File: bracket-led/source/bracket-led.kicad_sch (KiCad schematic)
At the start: 5 parts, among them J1 SM08B-SURS-TF(LF)(SN)

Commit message: production files added (i.e. gerber and dxf)
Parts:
- H1, H2: footprint Open Ephys: SLP3-150-100-R -> Open Ephys:BIVAR_SLP3-150-100-R
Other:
- moved on the sheet: H1, H2
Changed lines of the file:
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@@
     )
   )
-  (symbol (lib_id "Open Ephys:SLP3-150-100-R") (at 58.42 76.2 0) (unit 1)
+  (symbol (lib_id "Open Ephys:SLP3-150-100-R") (at 139.7 78.74 0) (unit 1)
     (in_bom yes) (on_board yes) (dnp no)
-    (property "Reference" "H2" (at 60.96 76.835 0)
+    (property "Reference" "H2" (at 142.24 79.375 0)
       (effects (font (size 1.27 1.27)) (justify left))
     )
-    (property "Value" "SLP3-150-100-R" (at 58.42 78.74 0)
+    (property "Value" "SLP3-150-100-R" (at 139.7 81.28 0)
       (effects (font (size 1.27 1.27)))
     )
-    (property "Footprint" "Open Ephys: SLP3-150-100-R" (at 58.42 76.2 0)
+    (property "Footprint" "Open Ephys:BIVAR_SLP3-150-100-R" (at 139.7 78.74 0)
       (effects (font (size 1.27 1.27)) hide)
     )
-    (property "Datasheet" "https://www.bivar.com/parts_content/Datasheets/SLP3-150-XXX-X.pdf" (at 58.42 76.2 0)
+    (property "Datasheet" "https://www.bivar.com/parts_content/Datasheets/SLP3-150-XXX-X.pdf" (at 139.7 78.74 0)
       (effects (font (size 1.27 1.27)) hide)
     )
@@
     )
   )
-  (symbol (lib_id "Open Ephys:SLP3-150-100-R") (at 58.42 53.34 0) (unit 1)
+  (symbol (lib_id "Open Ephys:SLP3-150-100-R") (at 139.7 50.8 0) (unit 1)
     (in_bom yes) (on_board yes) (dnp no)
-    (property "Reference" "H1" (at 60.96 53.975 0)
+    (property "Reference" "H1" (at 142.24 51.435 0)
       (effects (font (size 1.27 1.27)) (justify left))
     )
-    (property "Value" "SLP3-150-100-R" (at 58.42 55.88 0)
+    (property "Value" "SLP3-150-100-R" (at 139.7 53.34 0)
       (effects (font (size 1.27 1.27)))
     )
-    (property "Footprint" "Open Ephys: SLP3-150-100-R" (at 58.42 53.34 0)
+    (property "Footprint" "Open Ephys:BIVAR_SLP3-150-100-R" (at 139.7 50.8 0)
       (effects (font (size 1.27 1.27)) hide)
     )
-    (property "Datasheet" "https://www.bivar.com/parts_content/Datasheets/SLP3-150-XXX-X.pdf" (at 58.42 53.34 0)
+    (property "Datasheet" "https://www.bivar.com/parts_content/Datasheets/SLP3-150-XXX-X.pdf" (at 139.7 50.8 0)
       (effects (font (size 1.27 1.27)) hide)
     )
@@
     )
   )
-  (symbol (lib_id "power:GND") (at 115.57 80.01 90) (unit 1)
+  (symbol (lib_id "power:GND") (at 57.15 63.5 90) (unit 1)
     (in_bom yes) (on_board yes) (dnp no) (fields_autoplaced)
-    (property "Reference" "#PWR05" (at 121.92 80.01 0)
+    (property "Reference" "#PWR05" (at 63.5 63.5 0)
       (effects (font (size 1.27 1.27)) hide)
     )
-    (property "Value" "GND" (at 119.38 80.645 90)
+    (property "Value" "GND" (at 60.96 64.135 90)
       (effects (font (size 1.27 1.27)) (justify right))
     )
-    (property "Footprint" "" (at 115.57 80.01 0)
+    (property "Footprint" "" (at 57.15 63.5 0)
       (effects (font (size 1.27 1.27)) hide)
     )
-    (property "Datasheet" "" (at 115.57 80.01 0)
+    (property "Datasheet" "" (at 57.15 63.5 0)
       (effects (font (size 1.27 1.27)) hide)
     )
@@
       (effects (font (size 1.27 1.27)) hide)
     )
-    (property "Datasheet" "~" (at 115.57 63.5 0)
+    (property "Datasheet" "https://www.jst-mfg.com/product/pdf/eng/eSUR.pdf" (at 115.57 63.5 0)
       (effects (font (size 1.27 1.27)) hide)
     )
@@
     )
   )
-  (symbol (lib_id "power:PWR_FLAG") (at 115.57 80.01 90) (unit 1)
+  (symbol (lib_id "power:PWR_FLAG") (at 57.15 63.5 90) (unit 1)
     (in_bom yes) (on_board yes) (dnp no) (fields_autoplaced)
-    (property "Reference" "#FLG01" (at 113.665 80.01 0)
+    (property "Reference" "#FLG01" (at 55.245 63.5 0)
       (effects (font (size 1.27 1.27)) hide)
     )
-    (property "Value" "PWR_FLAG" (at 114.3 77.47 90)
+    (property "Value" "PWR_FLAG" (at 55.88 60.96 90)
       (effects (font (size 1.27 1.27)))
     )
-    (property "Footprint" "" (at 115.57 80.01 0)
+    (property "Footprint" "" (at 57.15 63.5 0)
       (effects (font (size 1.27 1.27)) hide)
     )
-    (property "Datasheet" "~" (at 115.57 80.01 0)
+    (property "Datasheet" "~" (at 57.15 63.5 0)
       (effects (font (size 1.27 1.27)) hide)
     )

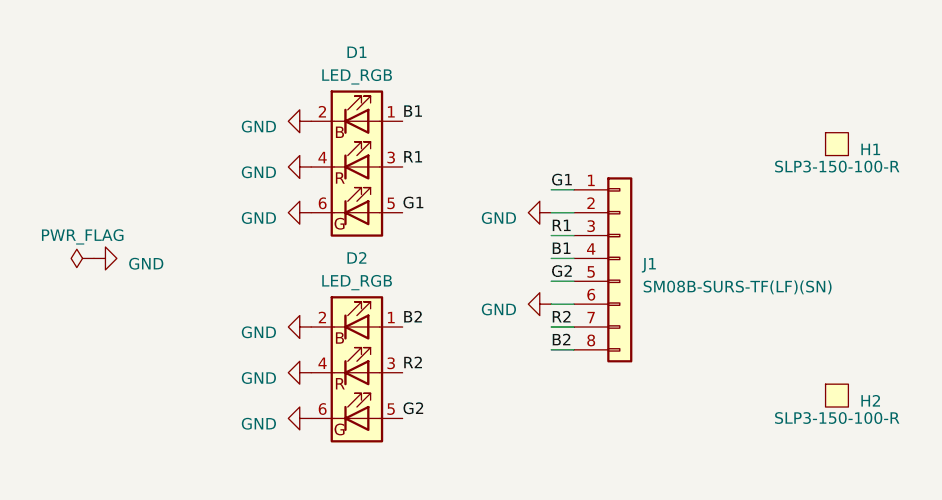
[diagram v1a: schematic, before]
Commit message: gerbers and kicad ready for review
gerber, bom, pnp files are in production folder for pcb fabrication and assembly. not sure if v-cut will be recognized by jlc. also, the individual pcbs are larger now with LEDs centered
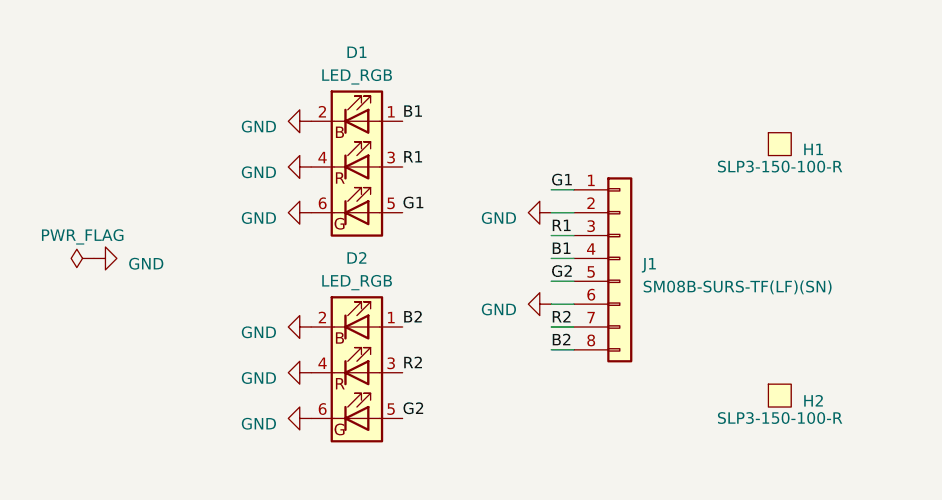
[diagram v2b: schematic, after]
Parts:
- D1, D2: LCSC (none) -> C131204
- J1: LCSC (none) -> C595161
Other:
- moved on the sheet: H1, H2
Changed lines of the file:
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@@
     )
   )
-  (symbol (lib_id "Open Ephys:SLP3-150-100-R") (at 139.7 78.74 0) (unit 1)
+  (symbol (lib_id "Open Ephys:SLP3-150-100-R") (at 133.35 78.74 0) (unit 1)
     (in_bom yes) (on_board yes) (dnp no)
-    (property "Reference" "H2" (at 142.24 79.375 0)
+    (property "Reference" "H2" (at 135.89 79.375 0)
       (effects (font (size 1.27 1.27)) (justify left))
     )
-    (property "Value" "SLP3-150-100-R" (at 139.7 81.28 0)
-      (effects (font (size 1.27 1.27)))
-    )
-    (property "Footprint" "Open Ephys:BIVAR_SLP3-150-100-R" (at 139.7 78.74 0)
-      (effects (font (size 1.27 1.27)) hide)
-    )
-    (property "Datasheet" "https://www.bivar.com/parts_content/Datasheets/SLP3-150-XXX-X.pdf" (at 139.7 78.74 0)
+    (property "Value" "SLP3-150-100-R" (at 133.35 81.28 0)
+      (effects (font (size 1.27 1.27)))
+    )
+    (property "Footprint" "Open Ephys:BIVAR_SLP3-150-100-R" (at 133.35 78.74 0)
+      (effects (font (size 1.27 1.27)) hide)
+    )
+    (property "Datasheet" "https://www.bivar.com/parts_content/Datasheets/SLP3-150-XXX-X.pdf" (at 133.35 78.74 0)
       (effects (font (size 1.27 1.27)) hide)
     )
@@
     )
   )
-  (symbol (lib_id "Open Ephys:SLP3-150-100-R") (at 139.7 50.8 0) (unit 1)
+  (symbol (lib_id "Open Ephys:SLP3-150-100-R") (at 133.35 50.8 0) (unit 1)
     (in_bom yes) (on_board yes) (dnp no)
-    (property "Reference" "H1" (at 142.24 51.435 0)
+    (property "Reference" "H1" (at 135.89 51.435 0)
       (effects (font (size 1.27 1.27)) (justify left))
     )
-    (property "Value" "SLP3-150-100-R" (at 139.7 53.34 0)
-      (effects (font (size 1.27 1.27)))
-    )
-    (property "Footprint" "Open Ephys:BIVAR_SLP3-150-100-R" (at 139.7 50.8 0)
-      (effects (font (size 1.27 1.27)) hide)
-    )
-    (property "Datasheet" "https://www.bivar.com/parts_content/Datasheets/SLP3-150-XXX-X.pdf" (at 139.7 50.8 0)
+    (property "Value" "SLP3-150-100-R" (at 133.35 53.34 0)
+      (effects (font (size 1.27 1.27)))
+    )
+    (property "Footprint" "Open Ephys:BIVAR_SLP3-150-100-R" (at 133.35 50.8 0)
+      (effects (font (size 1.27 1.27)) hide)
+    )
+    (property "Datasheet" "https://www.bivar.com/parts_content/Datasheets/SLP3-150-XXX-X.pdf" (at 133.35 50.8 0)
       (effects (font (size 1.27 1.27)) hide)
     )
@@
     )
     (property "Datasheet" "https://www.jst-mfg.com/product/pdf/eng/eSUR.pdf" (at 115.57 63.5 0)
+      (effects (font (size 1.27 1.27)) hide)
+    )
+    (property "LCSC" "C595161" (at 115.57 63.5 0)
       (effects (font (size 1.27 1.27)) hide)
     )
@@
       (effects (font (size 1.27 1.27)) hide)
     )
+    (property "LCSC" "C131204" (at 86.36 76.2 0)
+      (effects (font (size 1.27 1.27)) hide)
+    )
     (pin "1")
     (pin "2")
@@
       (effects (font (size 1.27 1.27)) hide)
     )
+    (property "LCSC" "C131204" (at 86.36 53.34 0)
+      (effects (font (size 1.27 1.27)) hide)
+    )

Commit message: fixed hole spacing, cleaned engraving
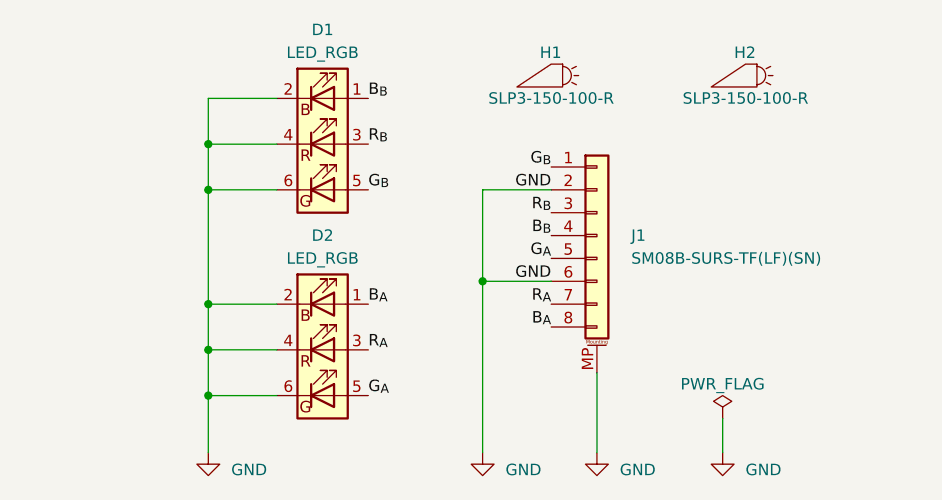
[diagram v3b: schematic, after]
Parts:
- removed J1: SM08B-SURS-TF(LF)(SN), Open Ephys:JST_SM08B-SURS-TF(LF)(SN), symbol Connector_Generic:Conn_01x08
- added J1: SM08B-SURS-TF(LF)(SN), Open Ephys:JST_SM08B-SURS-TF(LF)(SN), symbol Connector_Generic_MountingPin:Conn_01x08_MountingPin
- H1: renamed from H2; symbol Open Ephys:SLP3-150-100-R -> jonnew:LIGHTPIPE
- H2: renamed from H1; symbol Open Ephys:SLP3-150-100-R -> jonnew:LIGHTPIPE
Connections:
- net GND: now also J1.2 (Pin_2), J1.6 (Pin_6), J1.MP (MountPin)
- net B1 renamed B_{B}
- net B_{B}: now also J1.4 (Pin_4)
- net B2 renamed B_{A}
- net B_{A}: now also J1.8 (Pin_8)
- net G1 renamed G_{B}
- net G_{B}: now also J1.1 (Pin_1)
- net G2 renamed G_{A}
- net G_{A}: now also J1.5 (Pin_5)
- net R1 renamed R_{B}
- net R_{B}: now also J1.3 (Pin_3)
- net R2 renamed R_{A}
- net R_{A}: now also J1.7 (Pin_7)
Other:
- moved on the sheet: D1, D2
